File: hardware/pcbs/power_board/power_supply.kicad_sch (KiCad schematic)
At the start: 25 parts, among them J13 Barrel Jack, J14 ScrewTerminal_02, U13 LMR38020, U14 LMR38020

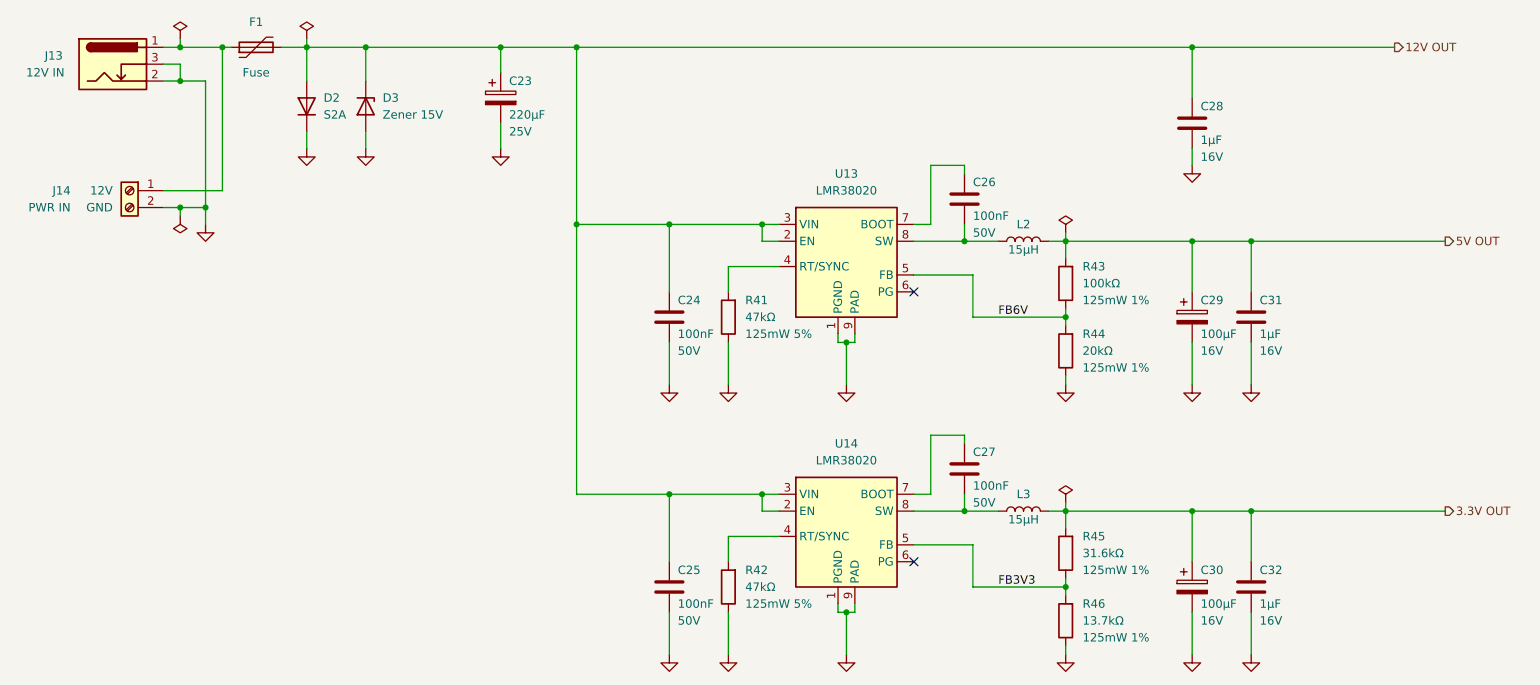
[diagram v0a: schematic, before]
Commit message: boards: fix many silly bugs discovered during testing
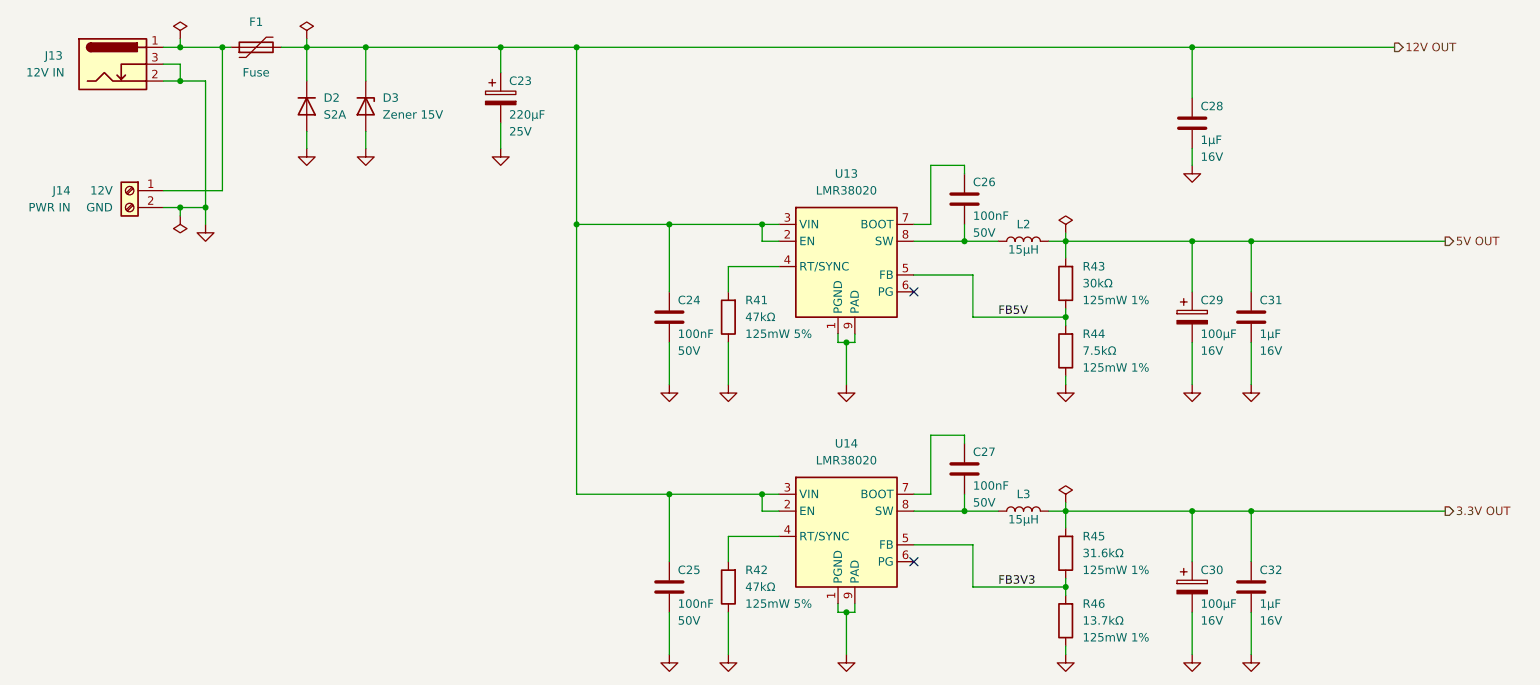
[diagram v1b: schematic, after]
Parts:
- R43: value 100kΩ -> 30kΩ; LCSC C149504 -> (none); Part R 100kΩ 125mW 1% 0805 -> R 30kΩ 125mW 1% 0805; Shop https://store.comet.bg/Catalogue/Product/24862/ -> https://store.comet.bg/Catalogue/Product/3554/
- R44: value 20kΩ -> 7.5kΩ; LCSC C4328 -> (none); Part R 20kΩ 125mW 1% 0805 -> R 7.5kΩ 125mW 1% 0805; Shop https://store.comet.bg/Catalogue/Product/29761/ -> https://store.comet.bg/Catalogue/Product/3545/
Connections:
- net 12V OUT: now also D2.1 (K); no longer D2.2 (A)
- net GND: now also D2.2 (A); no longer D2.1 (K)
- net FB6V renamed FB5V
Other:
- moved on the sheet: D2
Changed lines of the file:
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@@
 		)
 	)
-	(label "FB6V"
+	(label "FB5V"
 		(at 177.8 92.71 0)
 		(fields_autoplaced yes)
@@
 			)
 		)
-		(property "Value" "20kΩ"
+		(property "Value" "7.5kΩ"
 			(at 190.5 97.79 0)
 			(effects
@@
 			)
 		)
-		(property "Shop" "https://store.comet.bg/Catalogue/Product/29761/"
+		(property "Shop" "https://store.comet.bg/Catalogue/Product/3545/"
 			(at 187.96 97.79 0)
 			(effects
@@
 			)
 		)
-		(property "LCSC" "C4328"
+		(property "LCSC" ""
 			(at 187.96 97.79 0)
 			(effects
@@
 			)
 		)
-		(property "Part" "R 20kΩ 125mW 1% 0805"
+		(property "Part" "R 7.5kΩ 125mW 1% 0805"
 			(at 187.96 97.79 0)
 			(effects
@@
 			)
 		)
-		(property "Value" "100kΩ"
+		(property "Value" "30kΩ"
 			(at 190.5 87.63 0)
 			(effects
@@
 			)
 		)
-		(property "Shop" "https://store.comet.bg/Catalogue/Product/24862/"
+		(property "Shop" "https://store.comet.bg/Catalogue/Product/3554/"
 			(at 187.96 87.63 0)
 			(effects
@@
 			)
 		)
-		(property "LCSC" "C149504"
+		(property "LCSC" ""
 			(at 187.96 87.63 0)
 			(effects
@@
 			)
 		)
-		(property "Part" "R 100kΩ 125mW 1% 0805"
+		(property "Part" "R 30kΩ 125mW 1% 0805"
 			(at 187.96 87.63 0)
 			(effects
@@
 	(symbol
 		(lib_id "Diode:1N4007")
-		(at 73.66 60.96 90)
+		(at 73.66 60.96 270)
 		(unit 1)
 		(exclude_from_sim no)
@@
 					(size 1.27 1.27)
 				)
-				(justify right)
+				(justify left)
 			)
 		)
@@
 					(size 1.27 1.27)
 				)
-				(justify right)
+				(justify left)
 			)
 		)
 		(property "Footprint" "Diode_SMD:D_SMB"
-			(at 78.105 60.96 0)
+			(at 69.215 60.96 0)
 			(effects
 				(font

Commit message: power_board: add capacitors for filtering fan power supply
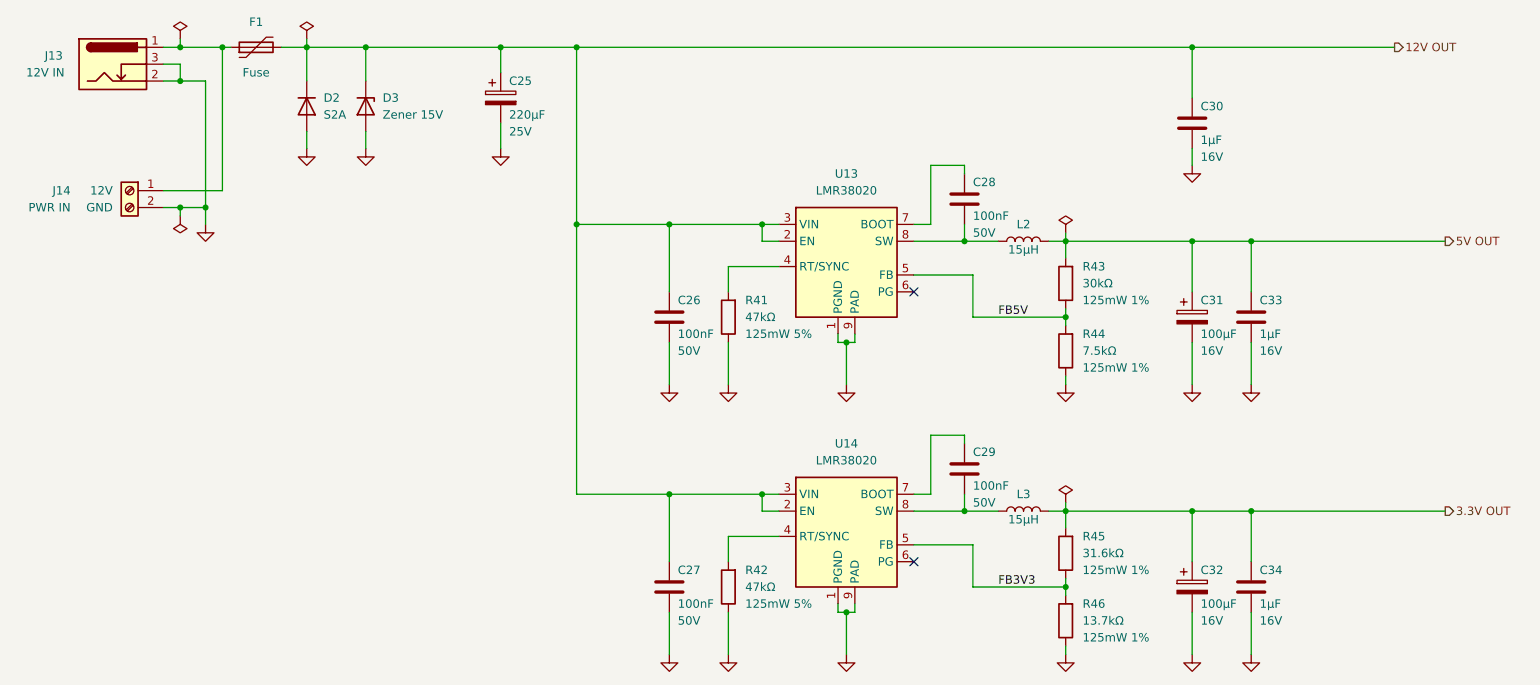
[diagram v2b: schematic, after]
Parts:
- renumbered C23 to C25, C24 to C26, C25 to C27, C26 to C28, C27 to C29, C28 to C30, C29 to C31, C30 to C32, C31 to C33, C32 to C34

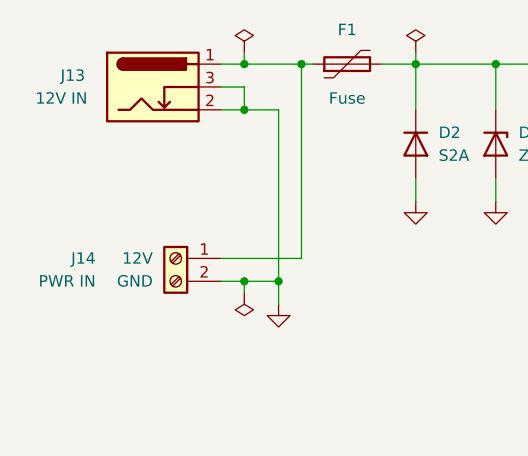
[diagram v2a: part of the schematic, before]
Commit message: power_board: flip 12V connectors
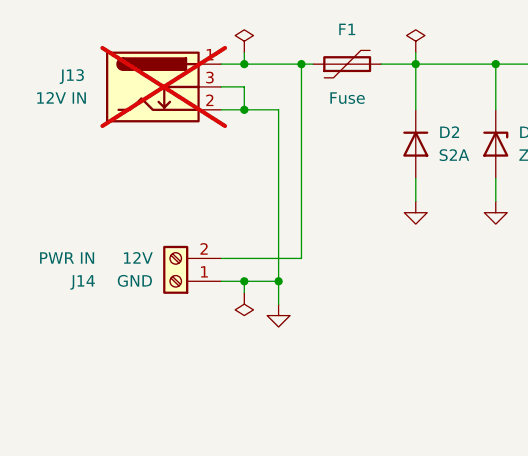
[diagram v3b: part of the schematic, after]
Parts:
- J13: now not fitted
- J14: Purpose Pin1 12V -> GND; Purpose Pin2 GND -> 12V
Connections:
- net GND: now also J14.1 (Pin_1); no longer J14.2 (Pin_2)
- net at F1.1, J13.1: now also J14.2 (Pin_2); no longer J14.1 (Pin_1)
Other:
- moved on the sheet: J14
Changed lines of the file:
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@@
 	(symbol
 		(lib_id "conn:Screw_Terminal_01x02")
-		(at 46.99 73.66 0)
-		(mirror y)
+		(at 46.99 76.2 180)
 		(unit 1)
 		(exclude_from_sim no)
@@
 		(dnp no)
 		(property "Reference" "J14"
+			(at 38.1 76.2 0)
+			(effects
+				(font
+					(size 1.27 1.27)
+				)
+				(justify left)
+			)
+		)
+		(property "Value" "ScrewTerminal_02"
+			(at 46.99 71.12 0)
+			(effects
+				(font
+					(size 1.27 1.27)
+				)
+				(hide yes)
+			)
+		)
+		(property "Footprint" "conn:TerminalBlock_4Ucon_1x02_P3.50mm_Vertical"
+			(at 46.99 76.2 0)
+			(effects
+				(font
+					(size 1.27 1.27)
+				)
+				(hide yes)
+			)
+		)
+		(property "Datasheet" "~"
+			(at 46.99 76.2 0)
+			(effects
+				(font
+					(size 1.27 1.27)
+				)
+				(hide yes)
+			)
+		)
+		(property "Description" ""
+			(at 46.99 76.2 0)
+			(effects
+				(font
+					(size 1.27 1.27)
+				)
+				(hide yes)
+			)
+		)
+		(property "Purpose" "PWR IN"
 			(at 38.1 73.66 0)
 			(effects
@@
 			)
 		)
-		(property "Value" "ScrewTerminal_02"
-			(at 46.99 78.74 0)
-			(effects
-				(font
-					(size 1.27 1.27)
-				)
-				(hide yes)
-			)
-		)
-		(property "Footprint" "conn:TerminalBlock_4Ucon_1x02_P3.50mm_Vertical"
-			(at 46.99 73.66 0)
-			(effects
-				(font
-					(size 1.27 1.27)
-				)
-				(hide yes)
-			)
-		)
-		(property "Datasheet" "~"
-			(at 46.99 73.66 0)
-			(effects
-				(font
-					(size 1.27 1.27)
-				)
-				(hide yes)
-			)
-		)
-		(property "Description" ""
-			(at 46.99 73.66 0)
-			(effects
-				(font
-					(size 1.27 1.27)
-				)
-				(hide yes)
-			)
-		)
-		(property "Purpose" "PWR IN"
-			(at 38.1 76.2 0)
+		(property "Purpose Pin1" "GND"
+			(at 44.45 76.2 0)
 			(effects
 				(font
@@
 			)
 		)
-		(property "Purpose Pin1" "12V"
+		(property "Purpose Pin2" "12V"
 			(at 44.45 73.66 0)
 			(effects
@@
 			)
 		)
-		(property "Purpose Pin2" "GND"
-			(at 44.45 76.2 0)
-			(effects
-				(font
-					(size 1.27 1.27)
-				)
-				(justify left)
-			)
-		)
 		(property "Shop" "https://store.comet.bg/Catalogue/Product/45040/ and https://store.comet.bg/Catalogue/Product/45028/"
-			(at 46.99 73.66 0)
+			(at 46.99 76.2 0)
 			(effects
 				(font
@@
 		)
 		(property "Part" "15EDGVC-3.5-02P-14-00AH, 15EDGKA-3.5-02P-14-100AH"
-			(at 46.99 73.66 0)
+			(at 46.99 76.2 0)
 			(effects
 				(font
@@
 		(in_bom yes)
 		(on_board yes)
-		(dnp no)
+		(dnp yes)
 		(property "Reference" "J13"
 			(at 35.56 53.34 0)

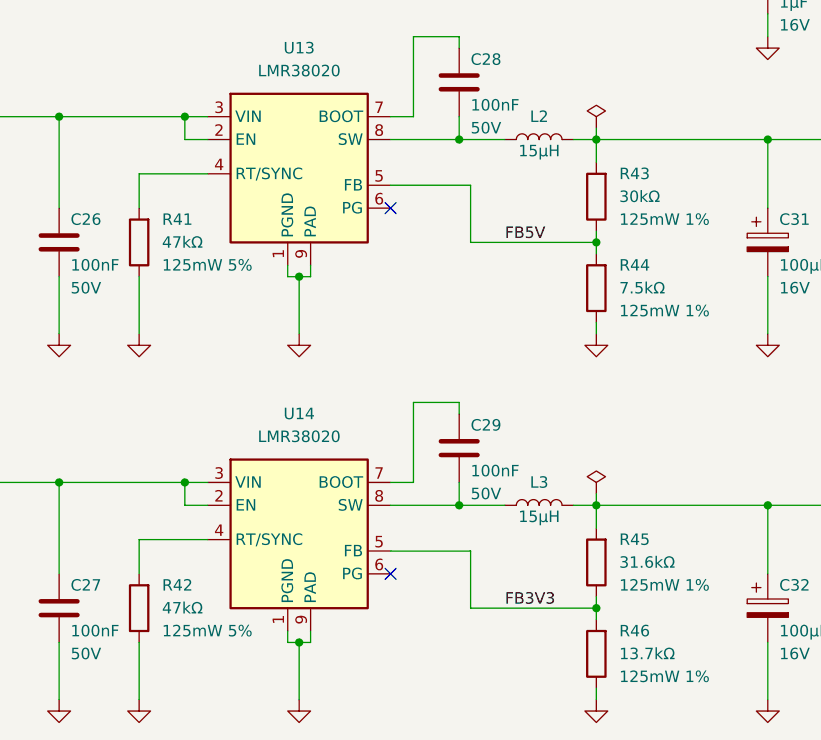
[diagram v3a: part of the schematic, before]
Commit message: power_board: use USB3-A passthrough connector and fix chg EN
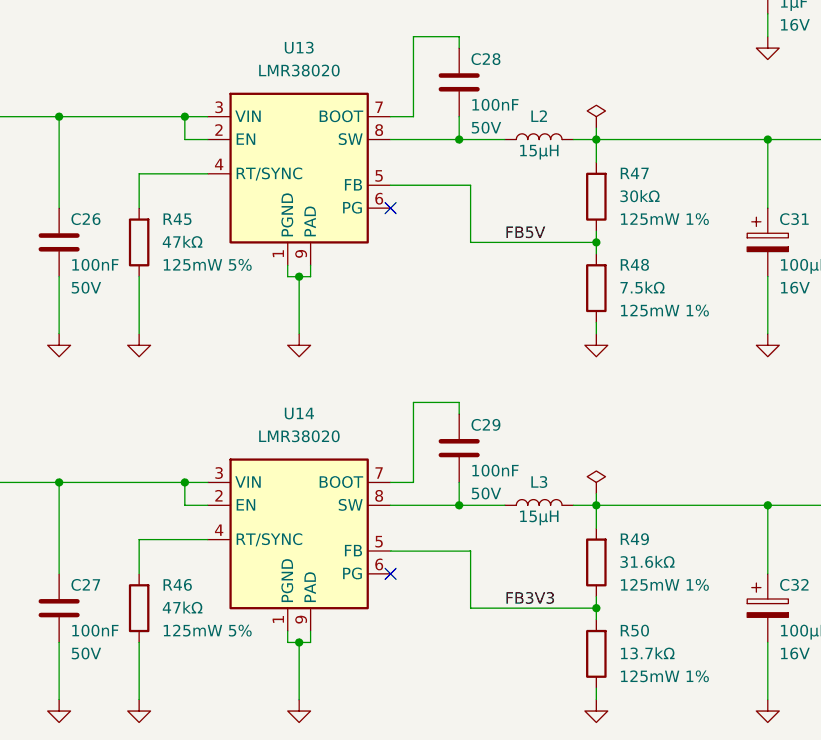
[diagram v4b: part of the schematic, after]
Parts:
- renumbered R41 to R45, R42 to R46, R43 to R47, R44 to R48, R45 to R49, R46 to R50
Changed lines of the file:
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@@
 		(on_board yes)
 		(dnp no)
-		(property "Reference" "R45"
+		(property "Reference" "R49"
 			(at 190.5 125.73 0)
 			(effects
@@
 			(project "power_board"
 				(path "/4b166175-80a4-48c6-994d-6e62a6160b87/61c6854b-d478-45fd-8007-466db156e311"
-					(reference "R45")
+					(reference "R49")
 					(unit 1)
 				)
@@
 		(on_board yes)
 		(dnp no)
-		(property "Reference" "R44"
+		(property "Reference" "R48"
 			(at 190.5 95.25 0)
 			(effects
@@
 			(project "power_board"
 				(path "/4b166175-80a4-48c6-994d-6e62a6160b87/61c6854b-d478-45fd-8007-466db156e311"
-					(reference "R44")
+					(reference "R48")
 					(unit 1)
 				)
@@
 		(on_board yes)
 		(dnp no)
-		(property "Reference" "R46"
+		(property "Reference" "R50"
 			(at 190.5 135.89 0)
 			(effects
@@
 			(project "power_board"
 				(path "/4b166175-80a4-48c6-994d-6e62a6160b87/61c6854b-d478-45fd-8007-466db156e311"
-					(reference "R46")
+					(reference "R50")
 					(unit 1)
 				)
@@
 		(on_board yes)
 		(dnp no)
-		(property "Reference" "R41"
+		(property "Reference" "R45"
 			(at 139.7 90.17 0)
 			(effects
@@
 			(project "power_board"
 				(path "/4b166175-80a4-48c6-994d-6e62a6160b87/61c6854b-d478-45fd-8007-466db156e311"
-					(reference "R41")
+					(reference "R45")
 					(unit 1)
 				)
@@
 		(on_board yes)
 		(dnp no)
-		(property "Reference" "R43"
+		(property "Reference" "R47"
 			(at 190.5 85.09 0)
 			(effects
@@
 			(project "power_board"
 				(path "/4b166175-80a4-48c6-994d-6e62a6160b87/61c6854b-d478-45fd-8007-466db156e311"
-					(reference "R43")
+					(reference "R47")
 					(unit 1)
 				)
@@
 		(on_board yes)
 		(dnp no)
-		(property "Reference" "R42"
+		(property "Reference" "R46"
 			(at 139.7 130.81 0)
 			(effects
@@
 			(project "power_board"
 				(path "/4b166175-80a4-48c6-994d-6e62a6160b87/61c6854b-d478-45fd-8007-466db156e311"
-					(reference "R42")
-					(unit 1)
-				)
+					(reference "R46")
+					(unit 1)
+				)

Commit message: power_board: add protection resistor to overload signal
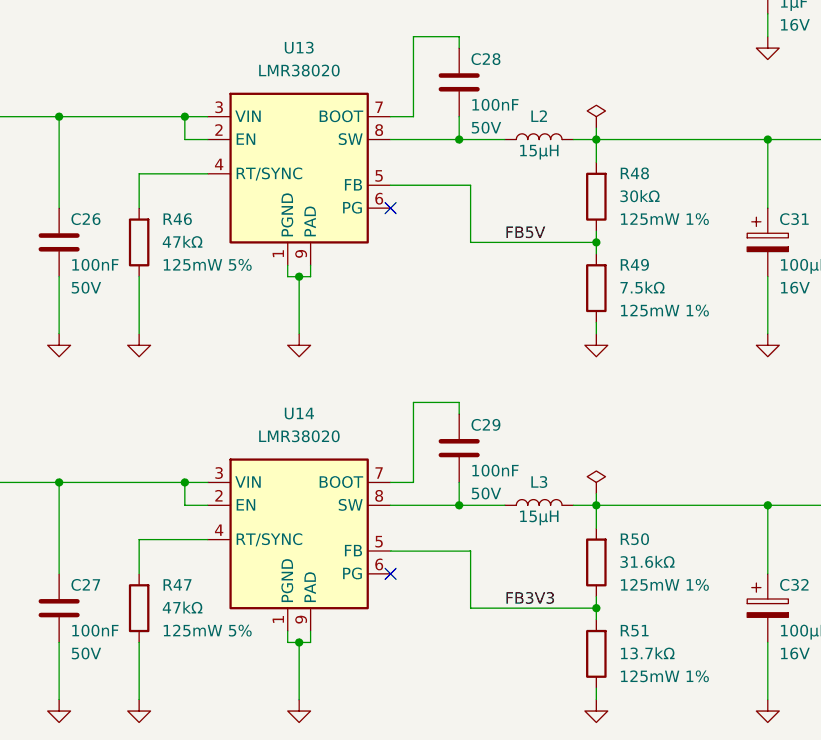
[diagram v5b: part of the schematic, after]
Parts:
- renumbered R45 to R46, R46 to R47, R47 to R48, R48 to R49, R49 to R50, R50 to R51
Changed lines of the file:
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@@
 		(on_board yes)
 		(dnp no)
-		(property "Reference" "R49"
+		(property "Reference" "R50"
 			(at 190.5 125.73 0)
 			(effects
@@
 			(project "power_board"
 				(path "/4b166175-80a4-48c6-994d-6e62a6160b87/61c6854b-d478-45fd-8007-466db156e311"
-					(reference "R49")
+					(reference "R50")
 					(unit 1)
 				)
@@
 		(on_board yes)
 		(dnp no)
-		(property "Reference" "R48"
+		(property "Reference" "R49"
 			(at 190.5 95.25 0)
 			(effects
@@
 			(project "power_board"
 				(path "/4b166175-80a4-48c6-994d-6e62a6160b87/61c6854b-d478-45fd-8007-466db156e311"
-					(reference "R48")
+					(reference "R49")
 					(unit 1)
 				)
@@
 		(on_board yes)
 		(dnp no)
-		(property "Reference" "R50"
+		(property "Reference" "R51"
 			(at 190.5 135.89 0)
 			(effects
@@
 			(project "power_board"
 				(path "/4b166175-80a4-48c6-994d-6e62a6160b87/61c6854b-d478-45fd-8007-466db156e311"
-					(reference "R50")
+					(reference "R51")
 					(unit 1)
 				)
@@
 		(on_board yes)
 		(dnp no)
-		(property "Reference" "R45"
+		(property "Reference" "R46"
 			(at 139.7 90.17 0)
 			(effects
@@
 			(project "power_board"
 				(path "/4b166175-80a4-48c6-994d-6e62a6160b87/61c6854b-d478-45fd-8007-466db156e311"
-					(reference "R45")
+					(reference "R46")
 					(unit 1)
 				)
@@
 		(on_board yes)
 		(dnp no)
-		(property "Reference" "R47"
+		(property "Reference" "R48"
 			(at 190.5 85.09 0)
 			(effects
@@
 			(project "power_board"
 				(path "/4b166175-80a4-48c6-994d-6e62a6160b87/61c6854b-d478-45fd-8007-466db156e311"
-					(reference "R47")
+					(reference "R48")
 					(unit 1)
 				)
@@
 		(on_board yes)
 		(dnp no)
-		(property "Reference" "R46"
+		(property "Reference" "R47"
 			(at 139.7 130.81 0)
 			(effects
@@
 			(project "power_board"
 				(path "/4b166175-80a4-48c6-994d-6e62a6160b87/61c6854b-d478-45fd-8007-466db156e311"
-					(reference "R46")
-					(unit 1)
-				)
+					(reference "R47")
+					(unit 1)
+				)

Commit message: boards: update wrong shop links
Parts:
- C30, C33, C34: Shop https://store.comet.bg/Catalogue/Product/16789/ -> https://store.comet.bg/Catalogue/Product/6645/
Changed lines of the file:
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@@
 			)
 		)
-		(property "Shop" "https://store.comet.bg/Catalogue/Product/16789/"
+		(property "Shop" "https://store.comet.bg/Catalogue/Product/6645/"
 			(at 215.9 133.35 0)
 			(effects
@@
 			)
 		)
-		(property "Shop" "https://store.comet.bg/Catalogue/Product/16789/"
+		(property "Shop" "https://store.comet.bg/Catalogue/Product/6645/"
 			(at 207.01 63.5 0)
 			(effects
@@
 			)
 		)
-		(property "Shop" "https://store.comet.bg/Catalogue/Product/16789/"
+		(property "Shop" "https://store.comet.bg/Catalogue/Product/6645/"
 			(at 215.9 92.71 0)
 			(effects
